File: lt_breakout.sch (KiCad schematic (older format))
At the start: 3 parts

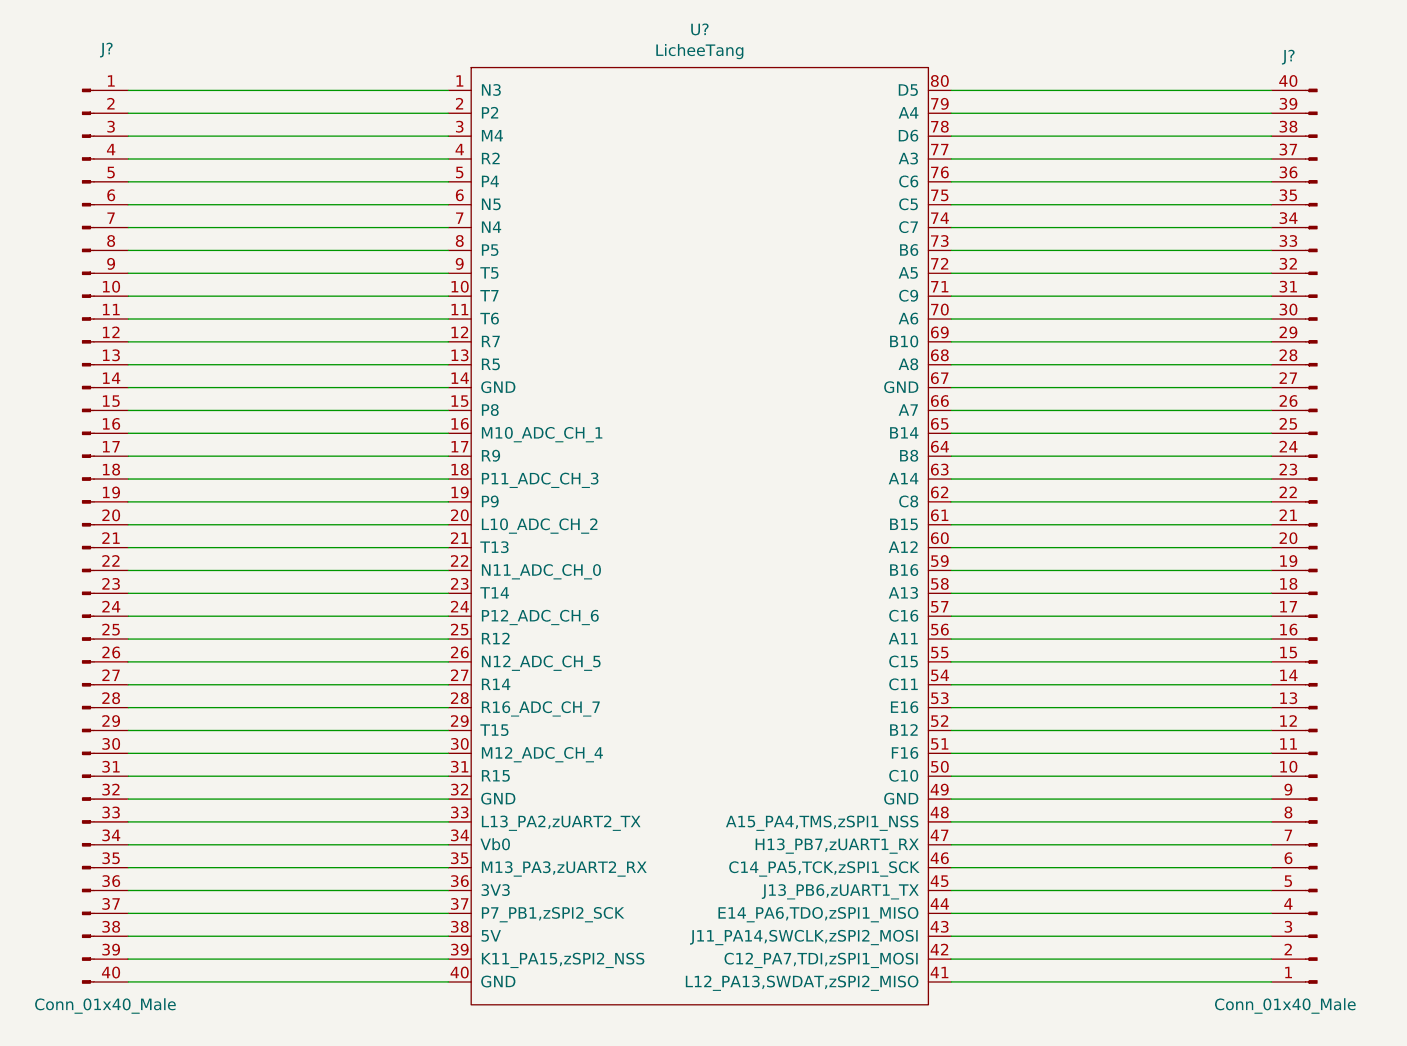
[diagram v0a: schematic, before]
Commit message: HDMI and VGA circuit added.
Signed-off-by: Kali Prasad <kprasadvnsi@protonmail.com>
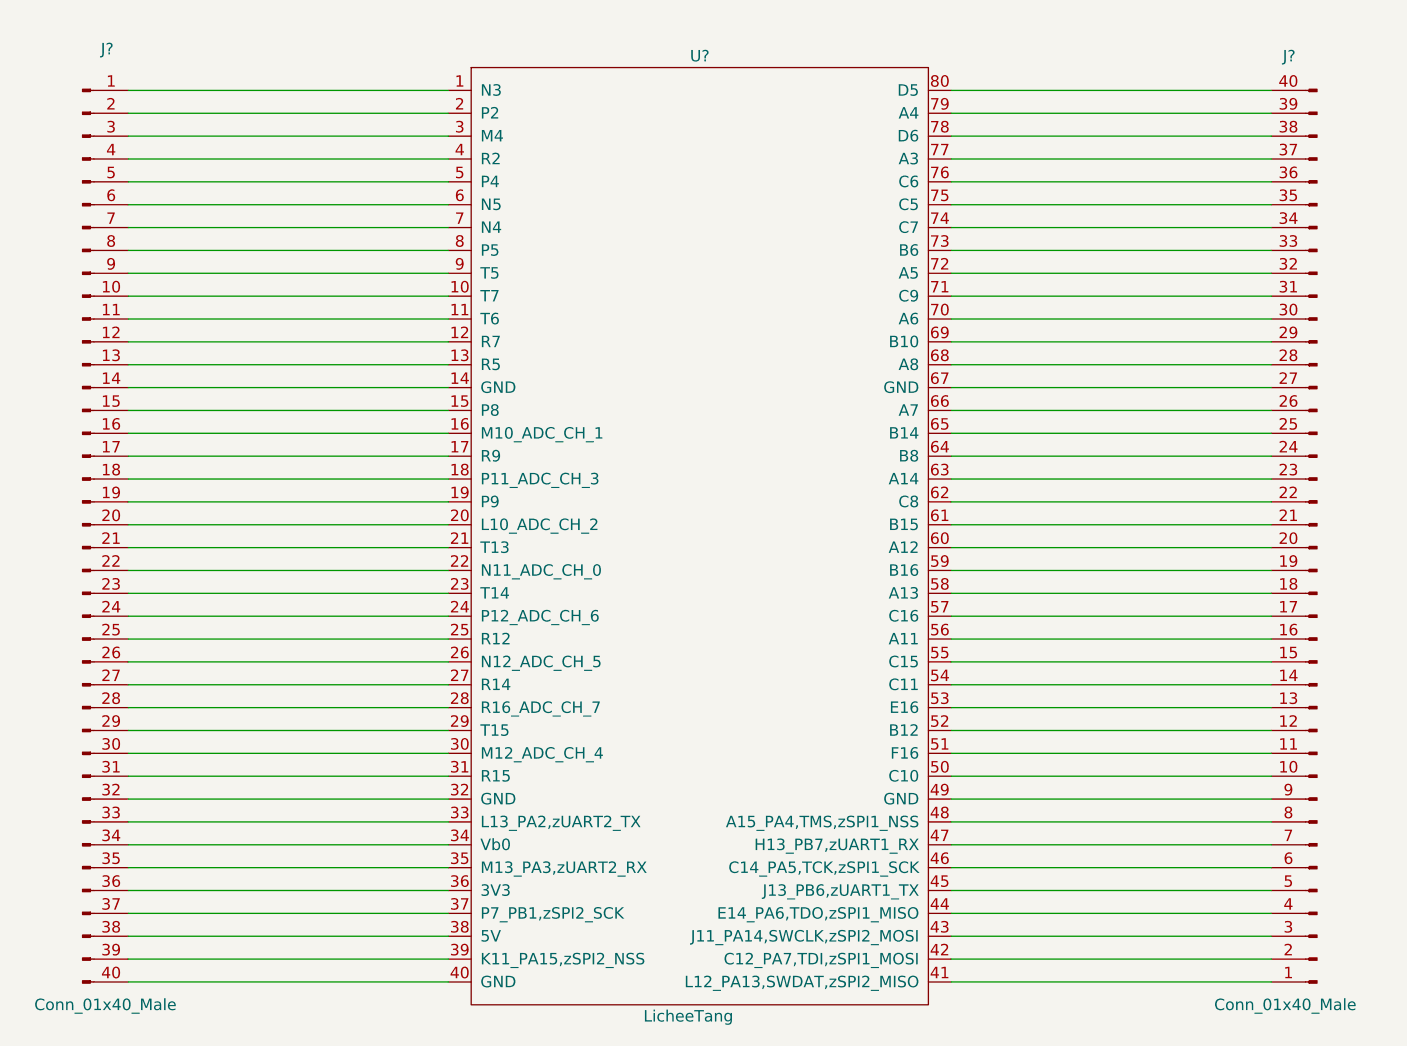
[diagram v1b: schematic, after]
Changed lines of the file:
@@
 U 1 1 5D0D3438
 P 5700 3800
-F 0 "U?" H 5700 6015 50  0000 C CNN
-F 1 "LicheeTang" H 5700 5924 50  0000 C CNN
+F 0 "U?" H 5700 5900 50  0000 C CNN
+F 1 "LicheeTang" H 5650 1700 50  0000 C CNN
 F 2 "" H 5200 4650 50  0001 C CNN
 F 3 "" H 5200 4650 50  0001 C CNN

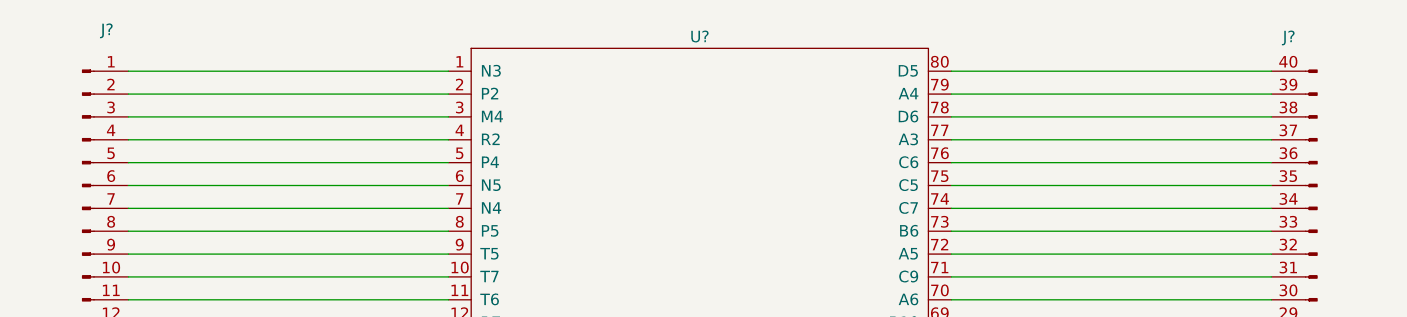
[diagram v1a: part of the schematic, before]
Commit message: SOM added.
Signed-off-by: Kali Prasad <kprasadvnsi@protonmail.com>
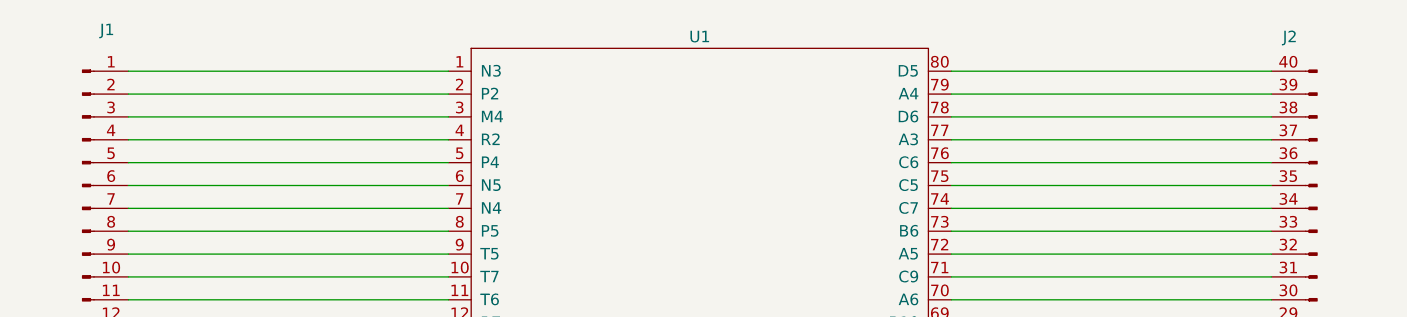
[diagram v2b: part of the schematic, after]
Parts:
- J1, J2: renamed from J?; footprint (none) -> Connector_PinHeader_2.54mm:PinHeader_2x20_P2.54mm_Vertical
- U1: renamed from U?; footprint (none) -> lt_eval_board:Lichee_Tang
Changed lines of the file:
@@
 $Descr A4 11693 8268
 encoding utf-8
-Sheet 2 7
+Sheet 2 8
 Title "LT_Eval_board"
 Date "2019-06-16"
@@
 $EndDescr
 $Comp
-L lt_eval_board:LicheeTang U?
+L lt_eval_board:LicheeTang U1
 U 1 1 5D0D3438
 P 5700 3800
-F 0 "U?" H 5700 5900 50  0000 C CNN
+F 0 "U1" H 5700 5900 50  0000 C CNN
 F 1 "LicheeTang" H 5650 1700 50  0000 C CNN
-F 2 "" H 5200 4650 50  0001 C CNN
+F 2 "lt_eval_board:Lichee_Tang" H 5200 4650 50  0001 C CNN
 F 3 "" H 5200 4650 50  0001 C CNN
 	1    5700 3800
@@
 $EndComp
 $Comp
-L Connector:Conn_01x40_Male J?
+L Connector:Conn_01x40_Male J1
 U 1 1 5D0EB726
 P 3000 3750
-F 0 "J?" H 3108 5831 50  0000 C CNN
+F 0 "J1" H 3108 5831 50  0000 C CNN
 F 1 "Conn_01x40_Male" H 3100 1650 50  0000 C CNN
-F 2 "" H 3000 3750 50  0001 C CNN
+F 2 "Connector_PinHeader_2.54mm:PinHeader_2x20_P2.54mm_Vertical" H 3000 3750 50  0001 C CNN
 F 3 "~" H 3000 3750 50  0001 C CNN
 	1    3000 3750
@@
 $EndComp
 $Comp
-L Connector:Conn_01x40_Male J?
+L Connector:Conn_01x40_Male J2
 U 1 1 5D0F701E
 P 8400 3850
-F 0 "J?" H 8550 1700 50  0000 R CNN
+F 0 "J2" H 8550 1700 50  0000 R CNN
 F 1 "Conn_01x40_Male" H 8850 5850 50  0000 R CNN
-F 2 "" H 8400 3850 50  0001 C CNN
+F 2 "Connector_PinHeader_2.54mm:PinHeader_2x20_P2.54mm_Vertical" H 8400 3850 50  0001 C CNN
 F 3 "~" H 8400 3850 50  0001 C CNN
 	1    8400 3850
